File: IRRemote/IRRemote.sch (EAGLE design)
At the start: 11 parts

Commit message: Various updates
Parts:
- U$3: value FOOTPRINTFOOTPRINT-2 -> DEVICE-PCB-TABS; device IntegerLabs:FOOTPRINTFOOTPRINT-2 -> Modulo:DEVICE-PCB-TABS; BOARD IR Remote -> (none); VERSION v1 -> (none)
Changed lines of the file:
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@@
 <part name="U$1" library="adafruit" deviceset="PNA460XM" device=""/>
 <part name="U$2" library="IntegerLabs" deviceset="TINY841" device=""/>
-<part name="U$3" library="IntegerLabs" deviceset="FOOTPRINT" device="FOOTPRINT-2">
-<attribute name="BOARD" value="IR Remote"/>
-<attribute name="VERSION" value="v1"/>
-</part>
+<part name="U$3" library="Modulo" deviceset="DEVICE-PCB" device="-TABS"/>
 <part name="C3" library="IntegerLabs" deviceset="CAP" device="0805" value=".47uF"/>
 <part name="R3" library="IntegerLabs" deviceset="RESISTOR" device="0805" value="680"/>
@@
 <segment>
 <pinref part="U$3" gate="G$1" pin="VCC"/>
-<wire x1="195.58" y1="25.4" x2="182.88" y2="25.4" width="0.1524" layer="91"/>
+<wire x1="193.04" y1="20.32" x2="182.88" y2="25.4" width="0.1524" layer="91"/>
 <label x="182.88" y="25.4" size="1.27" layer="95" rot="R180" xref="yes"/>
 </segment>
 <segment>
 <pinref part="U$3" gate="G$1" pin="VPROG"/>
-<wire x1="195.58" y1="17.78" x2="182.88" y2="17.78" width="0.1524" layer="91"/>
+<wire x1="193.04" y1="17.78" x2="182.88" y2="17.78" width="0.1524" layer="91"/>
 <label x="182.88" y="17.78" size="1.27" layer="95" rot="R180" xref="yes"/>
 </segment>
@@
 <segment>
 <pinref part="U$3" gate="G$1" pin="GND"/>
-<wire x1="195.58" y1="30.48" x2="182.88" y2="30.48" width="0.1524" layer="91"/>
+<wire x1="193.04" y1="7.62" x2="182.88" y2="30.48" width="0.1524" layer="91"/>
 <label x="182.88" y="30.48" size="1.27" layer="95" rot="R180" xref="yes"/>
 </segment>
@@
 <segment>
 <pinref part="U$3" gate="G$1" pin="RESET"/>
-<wire x1="195.58" y1="15.24" x2="182.88" y2="15.24" width="0.1524" layer="91"/>
+<wire x1="223.52" y1="17.78" x2="182.88" y2="15.24" width="0.1524" layer="91"/>
 <label x="182.88" y="15.24" size="1.27" layer="95" rot="R180" xref="yes"/>
 </segment>
@@
 <segment>
 <pinref part="U$3" gate="G$1" pin="MISO"/>
-<wire x1="195.58" y1="10.16" x2="182.88" y2="10.16" width="0.1524" layer="91"/>
+<wire x1="223.52" y1="20.32" x2="182.88" y2="10.16" width="0.1524" layer="91"/>
 <label x="182.88" y="10.16" size="1.27" layer="95" rot="R180" xref="yes"/>
 </segment>
@@
 <segment>
 <pinref part="U$3" gate="G$1" pin="SCL"/>
-<wire x1="195.58" y1="22.86" x2="182.88" y2="22.86" width="0.1524" layer="91"/>
+<wire x1="223.52" y1="12.7" x2="182.88" y2="22.86" width="0.1524" layer="91"/>
 <label x="182.88" y="22.86" size="1.27" layer="95" rot="R180" xref="yes"/>
 </segment>
 <segment>
 <pinref part="U$3" gate="G$1" pin="SCK"/>
-<wire x1="195.58" y1="12.7" x2="182.88" y2="12.7" width="0.1524" layer="91"/>
+<wire x1="223.52" y1="15.24" x2="182.88" y2="12.7" width="0.1524" layer="91"/>
 <label x="182.88" y="12.7" size="1.27" layer="95" rot="R180" xref="yes"/>
 </segment>
@@
 <segment>
 <pinref part="U$3" gate="G$1" pin="SDA"/>
-<wire x1="195.58" y1="27.94" x2="182.88" y2="27.94" width="0.1524" layer="91"/>
+<wire x1="223.52" y1="7.62" x2="182.88" y2="27.94" width="0.1524" layer="91"/>
 <label x="182.88" y="27.94" size="1.27" layer="95" rot="R180" xref="yes"/>
 </segment>
 <segment>
 <pinref part="U$3" gate="G$1" pin="MOSI"/>
-<wire x1="195.58" y1="7.62" x2="182.88" y2="7.62" width="0.1524" layer="91"/>
+<wire x1="223.52" y1="10.16" x2="182.88" y2="7.62" width="0.1524" layer="91"/>
 <label x="182.88" y="7.62" size="1.27" layer="95" rot="R180" xref="yes"/>
 </segment>

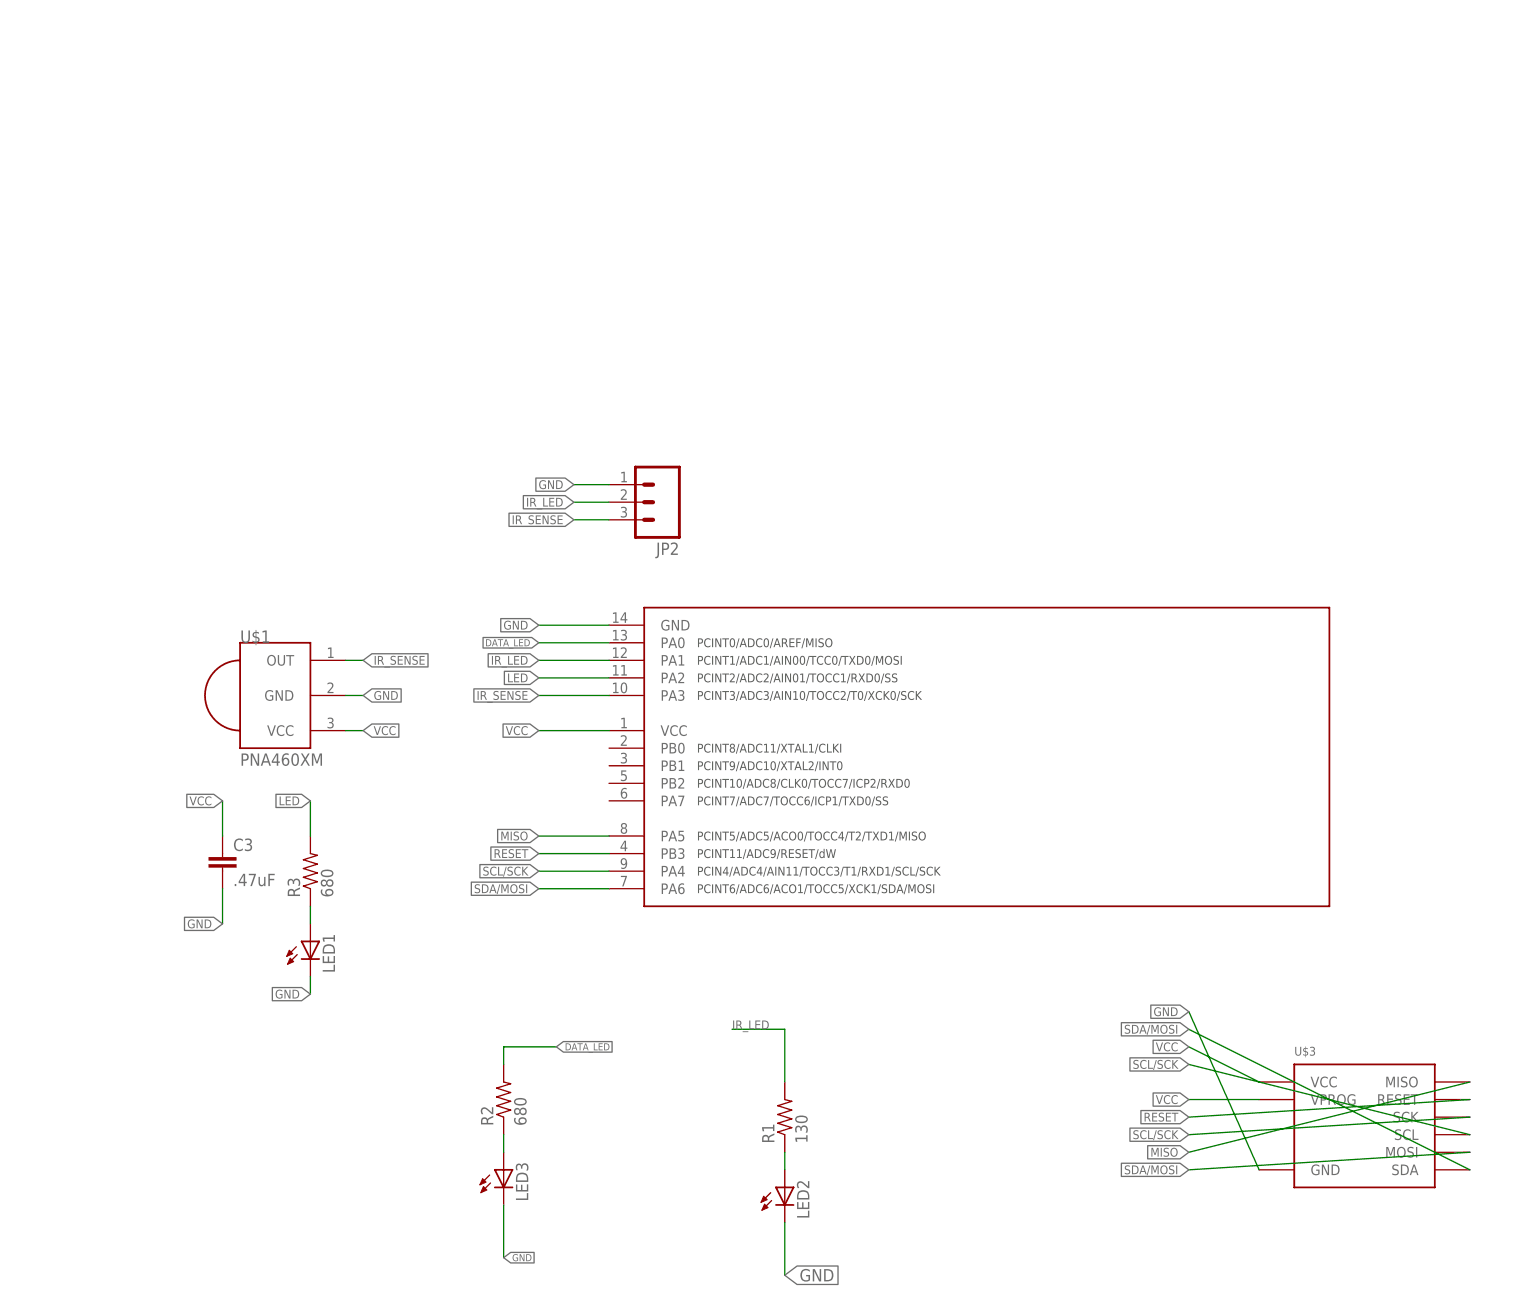
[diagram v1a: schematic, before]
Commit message: Major revision of all boards. Cleaned up old files. Exported BOM csv files for all boards
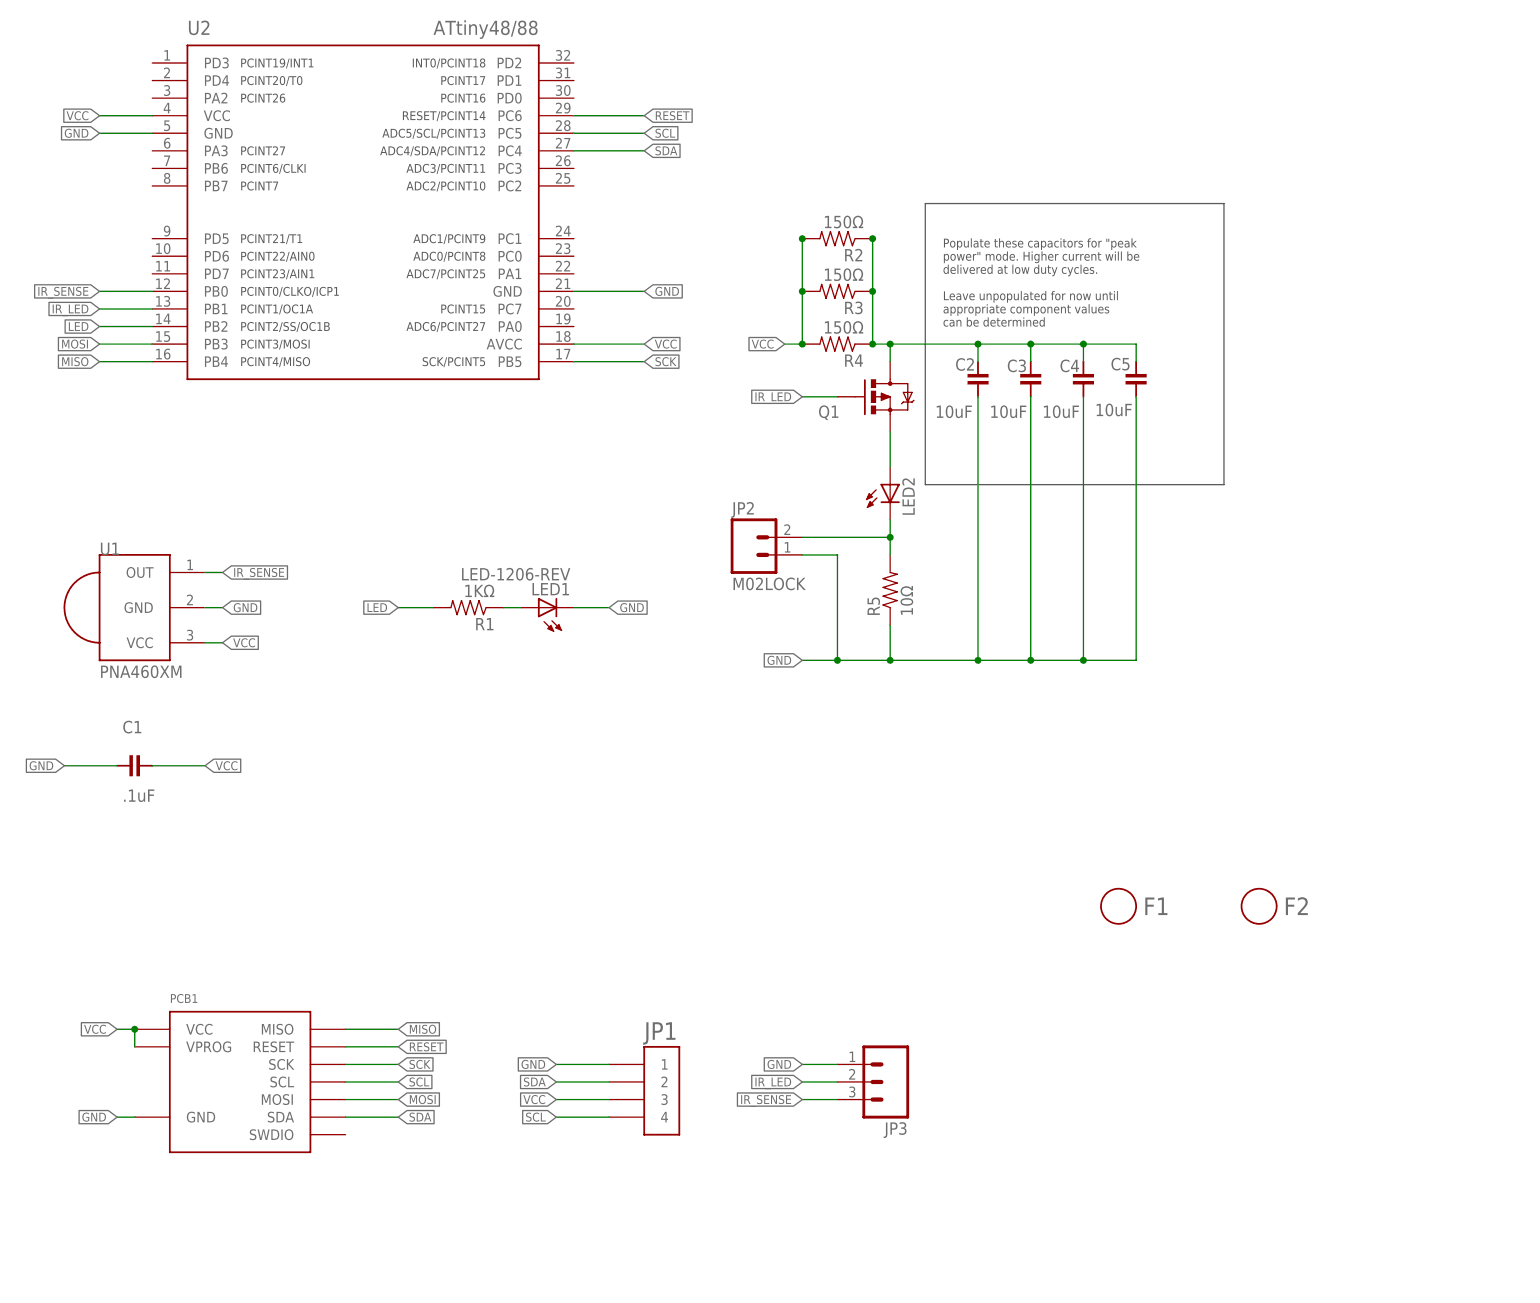
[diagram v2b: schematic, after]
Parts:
- removed LED3: (no value), adafruit:LEDCHIP-LED0805
- removed U$1: PNA460XM, adafruit:PNA460XM
- removed U$2: TINY841, IntegerLabs:TINY841
- removed U$3: DEVICE-PCB-TABS, Modulo:DEVICE-PCB-TABS
- added C1: .1uF, Modulo:CAPACITOR-.1UF
- added C2, C4, C5: 10uF, Modulo:CAPACITOR-10UF
- added F1, F2: FIDUCIAL, Modulo:FIDUCIAL
- added JP1: HEADER-1X4-AMPMODU, Modulo:HEADER-1X4-AMPMODU
- added JP3: (no value), SparkFun-Connectors:M03PTH
- added PCB1: DEVICE-PCB, Modulo:DEVICE-PCB
- added Q1: MOSFET-PCHANNELIRLML2244, SparkFun-DiscreteSemi:MOSFET-PCHANNELIRLML2244
- added R4: 150Ω, Modulo:RESISTOR-150Ω
- added R5: 10Ω, Modulo:RESISTOR-0603
- added U1: PNA460XM, adafruit:PNA460XM
- added U2: ATTINY48/88-TQFP, Modulo:ATTINY48/88-TQFP
- C3: value .47uF -> 10uF; device IntegerLabs:CAP0805 -> Modulo:CAPACITOR-10UF; BOM (none) -> EXCLUDE
- JP2: value (none) -> M02LOCK; device SparkFun-Connectors:M03PTH -> SparkFun-Connectors:M02LOCK; BOM (none) -> EXCLUDE
- LED1: value (none) -> LED-1206-REV; device adafruit:LEDCHIP-LED0805 -> Modulo:LED-1206-REV
- LED2: PARTNUM (none) -> IR928-6C-F
- R1: value 130 -> 1KΩ; device IntegerLabs:RESISTOR0805 -> Modulo:RESISTOR-1KΩ
- R2, R3: value 680 -> 150Ω; device IntegerLabs:RESISTOR0805 -> Modulo:RESISTOR-150Ω
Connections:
- removed net DATA_LED: R2.2, U$2.PA0
- removed net SCL/SCK: U$2.PA4, U$3.SCK, U$3.SCL
- removed net SDA/MOSI: U$2.PA6, U$3.MOSI, U$3.SDA
- new net MOSI: PCB1.MOSI, U2.PB3
- new net N$7: LED1.A, R1.1
- new net SCK: PCB1.SCK, U2.PB5
- new net SCL: JP1.4, PCB1.SCL, U2.PC5
- new net SDA: JP1.2, PCB1.SDA, U2.PC4
- net GND: now also C1.2, C2.2, C4.2, C5.2, JP1.1, JP3.1, PCB1.GND, R5.1, U1.GND, U2.GND, U2.GND@1; no longer LED2.C, LED3.C, U$1.GND, U$2.GND, U$3.GND
- net IR_LED: now also JP3.2, Q1.G, U2.PB1; no longer JP2.2, R1.2, U$2.PA1
- net IR_SENSE: now also JP3.3, U1.OUT, U2.PB0; no longer JP2.3, U$1.OUT, U$2.PA3
- net LED: now also R1.2, U2.PB2; no longer R3.2, U$2.PA2
- net MISO: now also PCB1.MISO, U2.PB4; no longer U$2.PA5, U$3.MISO
- net N$1: now also C2.1, C3.1, C4.1, C5.1, Q1.D, R3.1, R4.1; no longer LED3.A
- net N$2: now also JP2.2, LED2.C, R5.2; no longer LED1.A, R3.1
- net N$3: now also Q1.S; no longer R1.1
- net RESET: now also PCB1.RESET, U2.PC6; no longer U$2.PB3, U$3.RESET
- net VCC: now also C1.1, JP1.3, PCB1.VCC, PCB1.VPROG, R2.2, R3.2, R4.2, U1.VCC, U2.AVCC, U2.VCC; no longer C3.1, U$1.VCC, U$2.VCC, U$3.VCC, U$3.VPROG
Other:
- note added: "Populate these capacitors for "peak power" mode. Higher current will be delivered at low duty cycles. Leave unpopulated for now until appropriate component values can be determined"
- moved on the sheet: LED1, LED2, R1, R2, R3

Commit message: Check point of current PCB designs. Among other things I think this change includes rewiring of programming lines on many of the boards,.
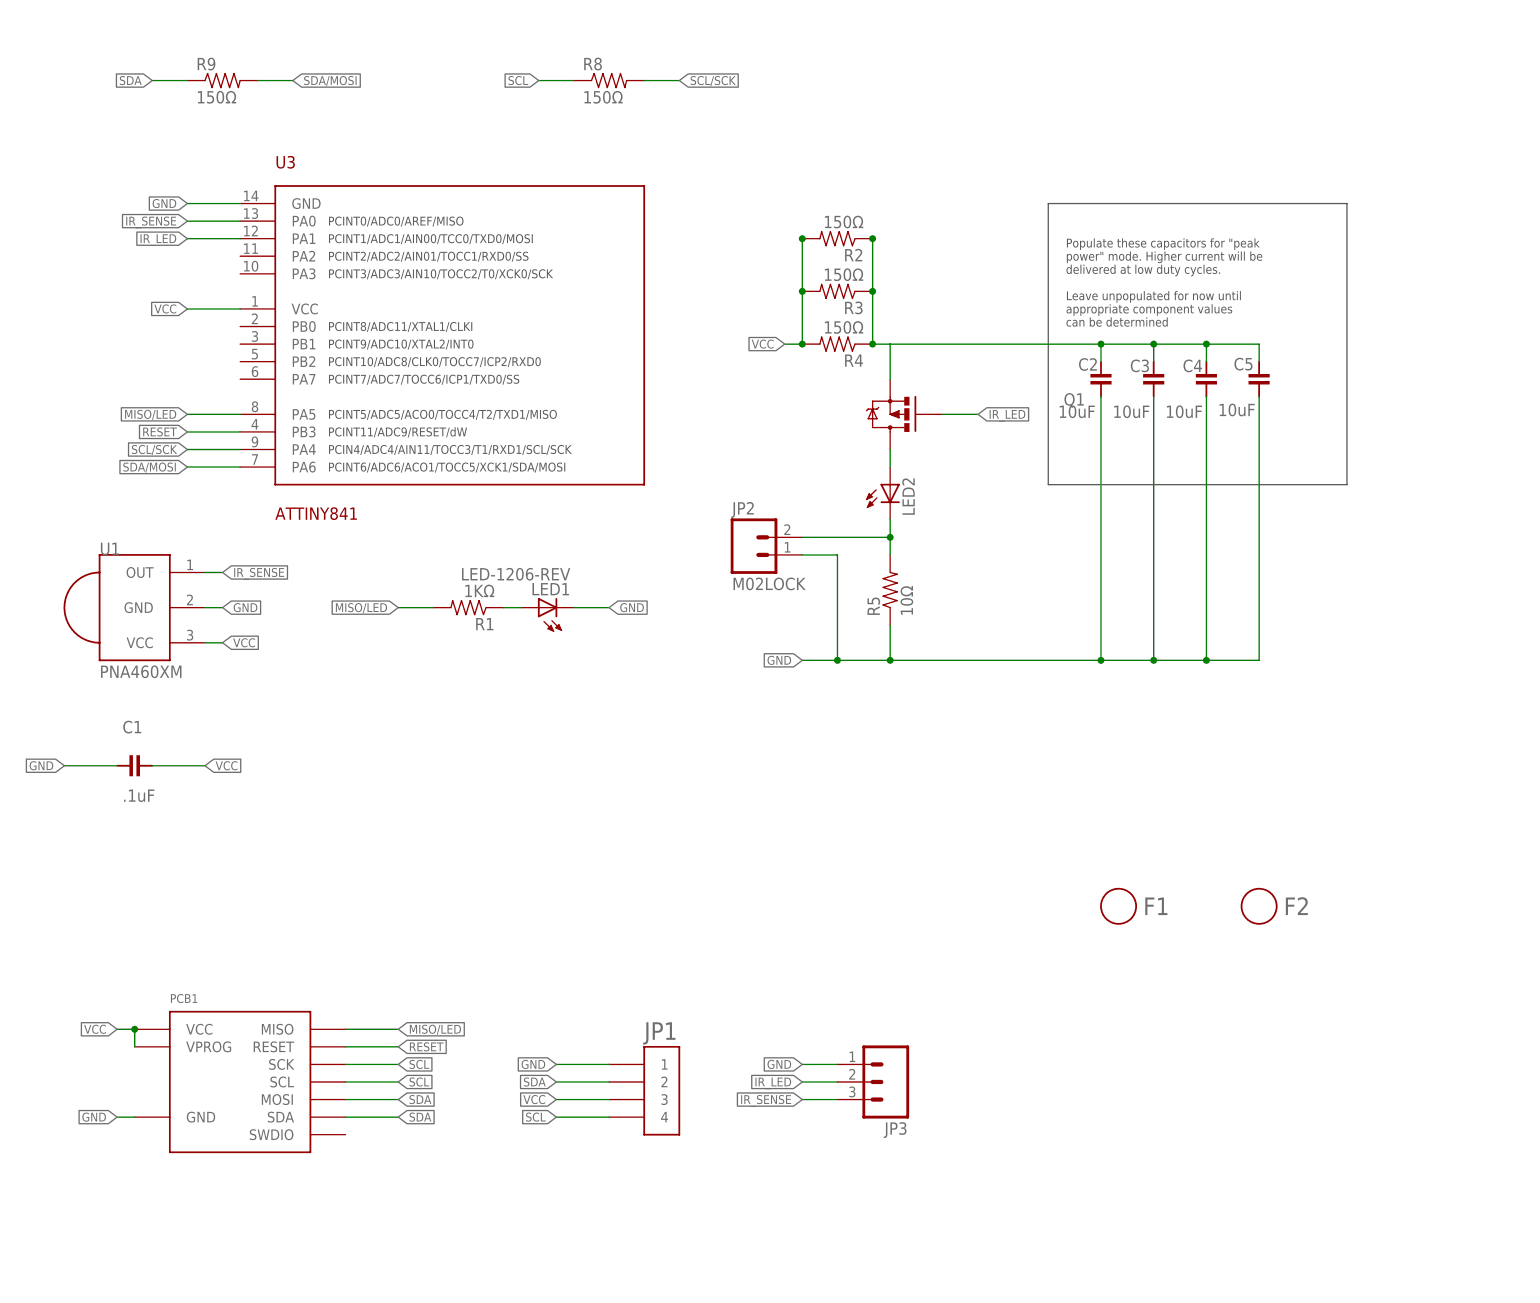
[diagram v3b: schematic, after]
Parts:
- removed U2: ATTINY48/88-TQFP, Modulo:ATTINY48/88-TQFP
- added R8, R9: 150Ω, Modulo:RESISTOR-150Ω
- added U3: ATTINY841, Modulo:ATTINY841
- Q1: PARTNUM DMG2305UX -> DMG2305UX-7
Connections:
- removed net LED: R1.2, U2.PB2
- removed net MISO: PCB1.MISO, U2.PB4
- removed net MOSI: PCB1.MOSI, U2.PB3
- removed net SCK: PCB1.SCK, U2.PB5
- new net MISO/LED: PCB1.MISO, R1.2, U3.PA5
- new net SCL/SCK: R8.2, U3.PA4
- new net SDA/MOSI: R9.2, U3.PA6
- net GND: now also U3.GND; no longer U2.GND, U2.GND@1
- net IR_LED: now also U3.PA1; no longer U2.PB1
- net IR_SENSE: now also U3.PA0; no longer U2.PB0
- net N$1: now also Q1.S; no longer Q1.D
- net N$3: now also Q1.D; no longer Q1.S
- net RESET: now also U3.PB3; no longer U2.PC6
- net SCL: now also PCB1.SCK, R8.1; no longer U2.PC5
- net SDA: now also PCB1.MOSI, R9.1; no longer U2.PC4
- net VCC: now also U3.VCC; no longer U2.AVCC, U2.VCC
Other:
- moved on the sheet: C2, C3, C4, C5, Q1

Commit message: Various changes
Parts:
- removed C2, C3, C4, C5: 10uF, Modulo:CAPACITOR-10UF
- removed JP2: M02LOCK, SparkFun-Connectors:M02LOCK
- removed Q1: MOSFET-PCHANNELIRLML2244, SparkFun-DiscreteSemi:MOSFET-PCHANNELIRLML2244
- added R6: 150Ω, Modulo:RESISTOR-150Ω
- R5: value 10Ω -> 150Ω; device Modulo:RESISTOR-0603 -> Modulo:RESISTOR-150Ω; PARTNUM ERJ-3EKF10R0V -> (none)
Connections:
- removed net N$1: C2.1, C3.1, C4.1, C5.1, Q1.S, R2.1, R3.1, R4.1
- removed net N$2: JP2.2, LED2.C, R5.2
- removed net N$3: LED2.A, Q1.D
- new net IR_LED1: R6.2, U3.PA1
- new net IR_LED2: R2.2, U3.PA3
- new net IR_LED3: R3.2, U3.PA7
- new net IR_LED4: R4.2, U3.PA2
- new net IR_LED5: R5.2, U3.PB2
- net GND: now also LED2.C; no longer C2.2, C3.2, C4.2, C5.2, JP2.1, R5.1
- net IR_LED: now also LED2.A, R2.1, R3.1, R4.1, R5.1, R6.1; no longer Q1.G, U3.PA1
- net VCC: no longer R2.2, R3.2, R4.2
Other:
- note removed: "Populate these capacitors for "peak power" mode. Higher current will be delivered at low duty cycles. Leave unpopulated for now until appropriate component values can be determined"
- moved on the sheet: R5

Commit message: Various small tweaks based on testing and feedback from manufacturer.
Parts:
- R8, R9: value 150Ω -> 0Ω; device Modulo:RESISTOR-150Ω -> Modulo:RESISTOR-0Ω
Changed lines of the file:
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@@
 <part name="R2" library="Modulo" deviceset="RESISTOR" device="-150Ω" value="150Ω"/>
 <part name="U3" library="Modulo" deviceset="ATTINY841" device="" value="ATTINY841"/>
-<part name="R8" library="Modulo" deviceset="RESISTOR" device="-150Ω" value="150Ω">
+<part name="R8" library="Modulo" deviceset="RESISTOR" device="-0Ω" value="0Ω">
 <attribute name="BOM" value="EXCLUDE"/>
 </part>
-<part name="R9" library="Modulo" deviceset="RESISTOR" device="-150Ω" value="150Ω">
+<part name="R9" library="Modulo" deviceset="RESISTOR" device="-0Ω" value="0Ω">
 <attribute name="BOM" value="EXCLUDE"/>
 </part>

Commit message: Various minor tweaks based on testing and feedback from manufacturer
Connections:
- net IR_LED: no longer JP3.2
- net IR_LED1: now also JP3.2
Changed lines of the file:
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@@
 <net name="IR_LED" class="0">
-<segment>
-<pinref part="JP3" gate="G$1" pin="2"/>
-<wire x1="132.08" y1="20.32" x2="127" y2="20.32" width="0.1524" layer="91"/>
-<label x="127" y="20.32" size="1.27" layer="95" rot="R180" xref="yes"/>
-</segment>
 <segment>
 <pinref part="LED2" gate="G$1" pin="A"/>
@@
 <label x="121.92" y="149.86" size="1.27" layer="95" rot="R180" xref="yes"/>
 </segment>
+<segment>
+<pinref part="JP3" gate="G$1" pin="2"/>
+<wire x1="132.08" y1="20.32" x2="127" y2="20.32" width="0.1524" layer="91"/>
+<label x="127" y="20.32" size="1.27" layer="95" rot="R180" xref="yes"/>
+</segment>
 </net>
